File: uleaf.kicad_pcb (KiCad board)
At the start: 4 copper layers, 25.7 x 26.3 mm, 26 parts, among them J2 SWD Debug, J3 Conn_01x10, J4 Conn_01x10, U2 PCM5102, U3 APS6404L-3SQRx-SN, U4 W25Q128JVS, U5 STM32H533CEUx, Y1 Crystal_GND24

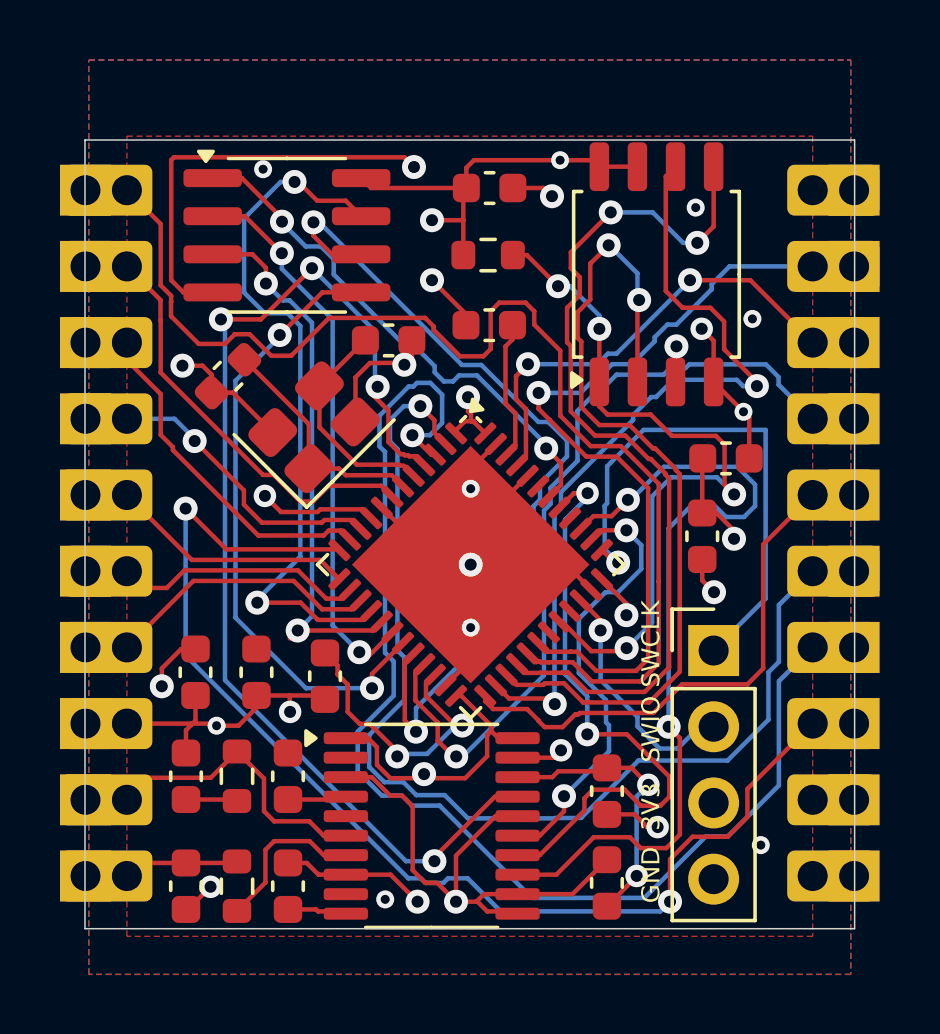
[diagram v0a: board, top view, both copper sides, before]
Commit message: Fixed problems with pcm connections, rev 0.4
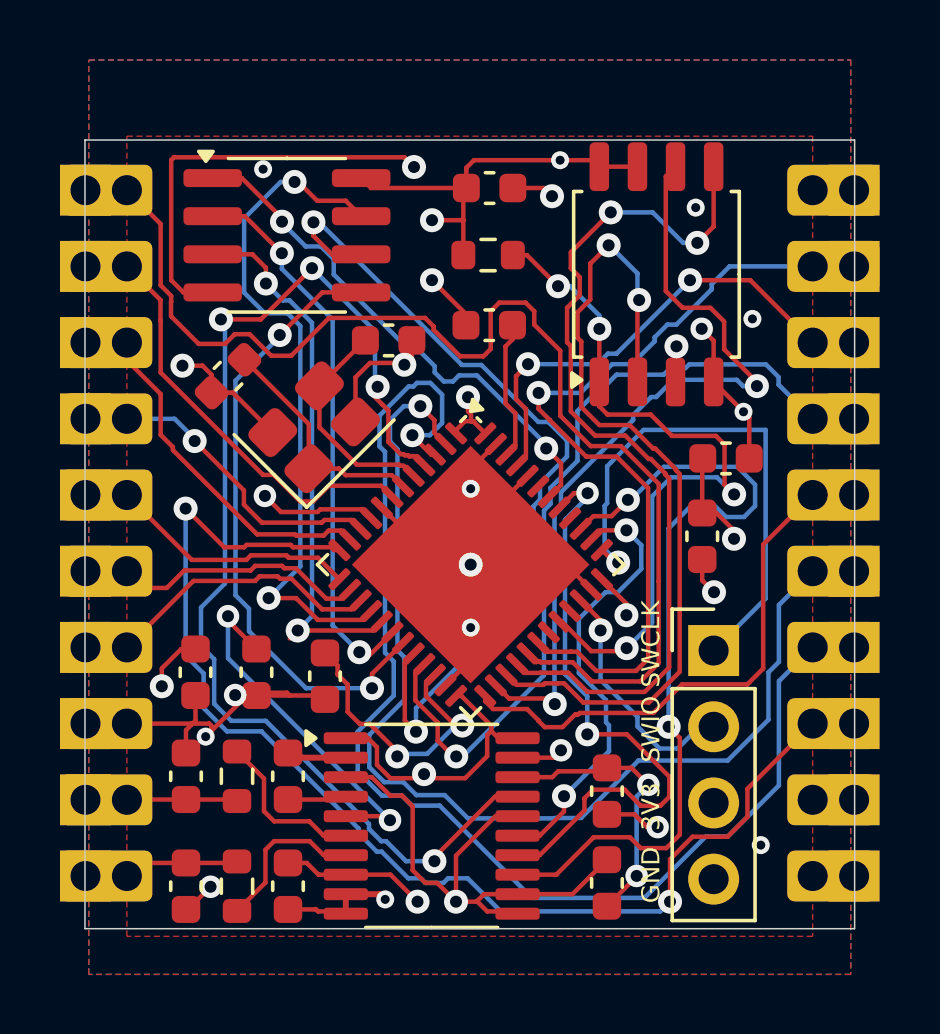
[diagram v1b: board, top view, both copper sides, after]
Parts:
- C16, C17: value 100n -> 27pF
- Y1: value Crystal_GND24 -> ABM8-25.000MHZ-B2
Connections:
- C6 pad 2: Net-(C6-Pad2) -> /OUT_L
- R2 pad 1: /OUT_L -> Net-(U2-OUTL)
- R2 pad 2: Net-(C6-Pad2) -> /OUT_L
- U2 pad 6: /OUT_L -> Net-(U2-OUTL)
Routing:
- net Net-(U2-VNEG): track 0.00 -> 12.1 mm, vias 0 -> 2
- net Net-(U2-OUTL): track 0.00 -> 5.43 mm
- net /OUT_L: track 9.76 -> 4.73 mm
- net GND: track 86.9 -> 90.7 mm
- net Net-(U2-CAPP): track 0.00 -> 1.99 mm
- net Net-(C6-Pad2): track 1.72 -> 0.00 mm
- net /PCM_MUTE_CONTROL: track 37.6 -> 39.1 mm
- net /PA2: track 39.1 -> 40.0 mm
- net /QUADSPI1_BK1_IO3: track 23.7 -> 23.0 mm
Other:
- board text added: "uLEAF rev 0.4"
- board text removed: "uLEAF rev 0.3"
